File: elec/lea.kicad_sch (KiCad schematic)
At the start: 9 parts, among them J1 Servomoteur, J2 Screw_Terminal_01x02, J3 Jack, SW1 SW_SPDT

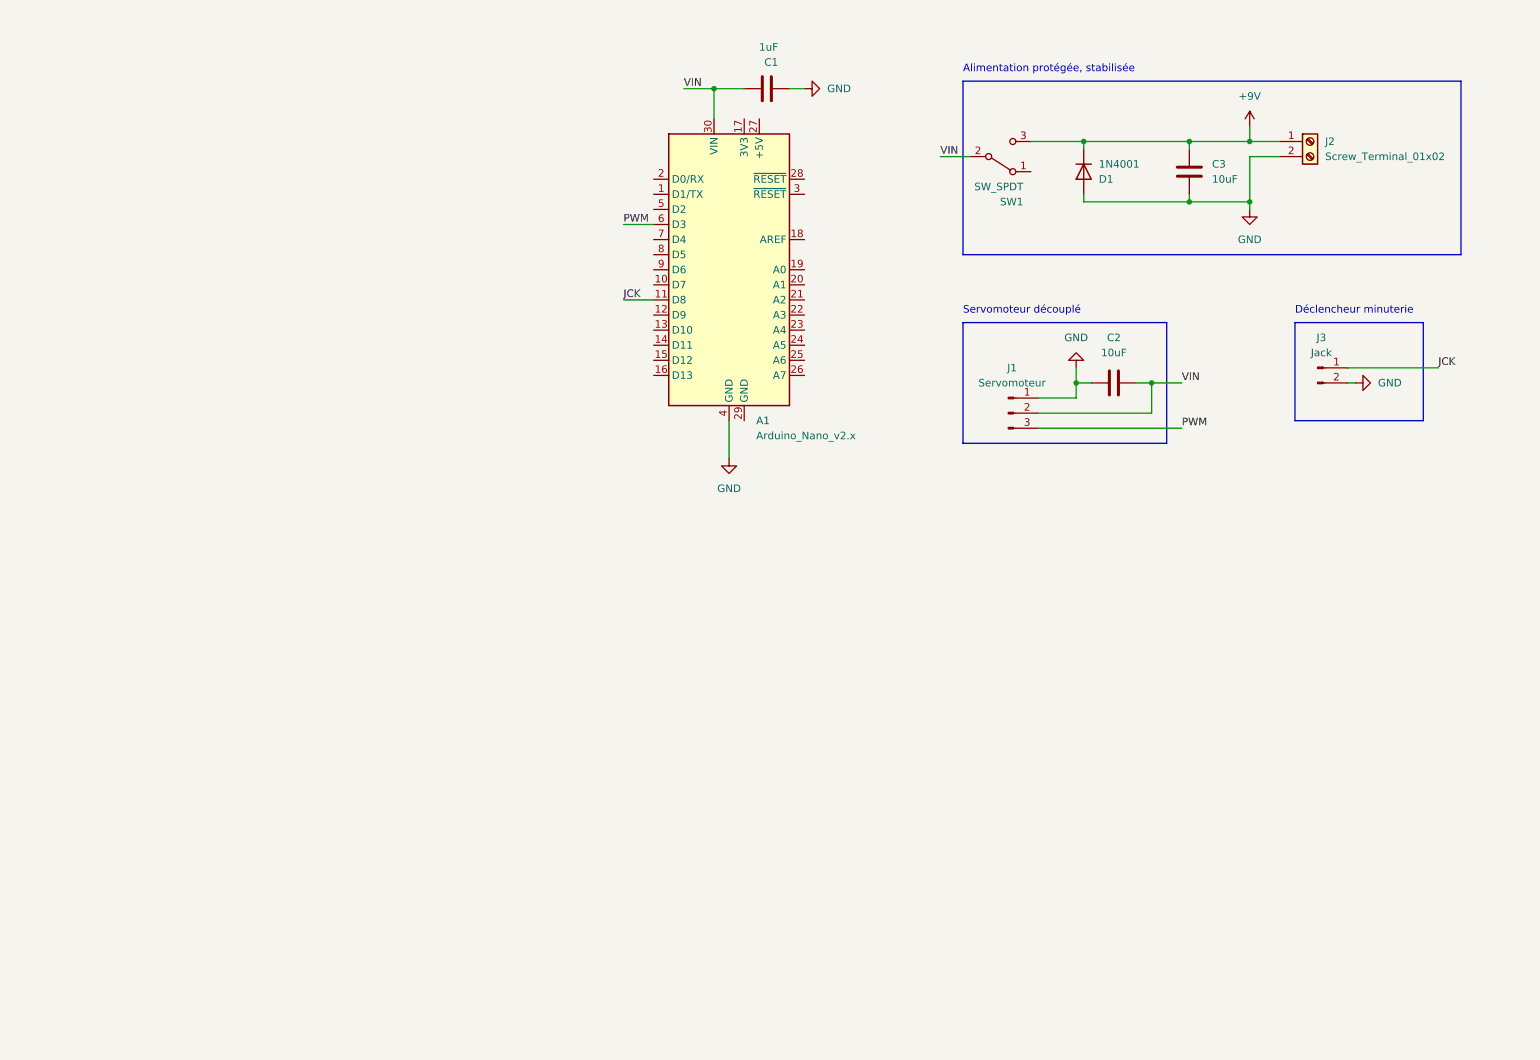
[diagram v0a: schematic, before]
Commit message: Refonte complète du circuit
- réagencement des composants sur le schéma
- pcb désormais rectangulaire
- ajout du régulateur de tension et de son empreinte
- masses séparées avec possibilité de pont
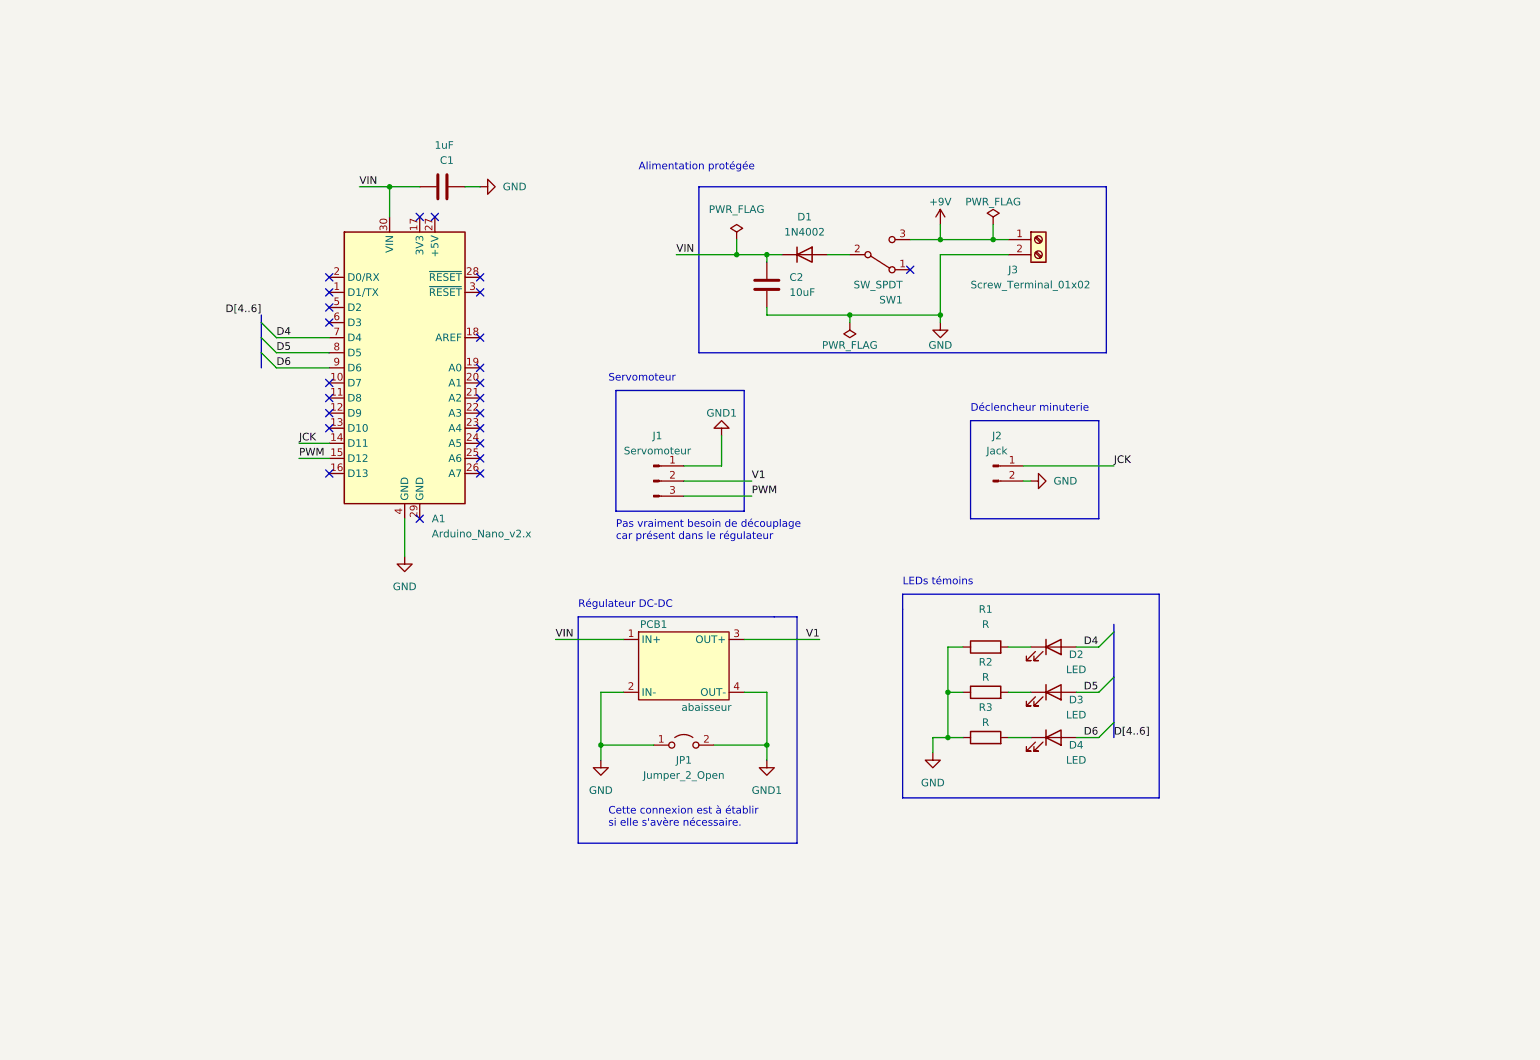
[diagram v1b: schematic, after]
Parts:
- removed C2: 10uF, Capacitor_THT:C_Radial_D6.3mm_H5.0mm_P2.50mm, symbol Device:C
- removed D1: 1N4001, Diode_THT:D_DO-41_SOD81_P10.16mm_Horizontal, symbol Diode:1N4001
- added D1: 1N4002, Diode_THT:D_DO-41_SOD81_P10.16mm_Horizontal, symbol Diode:1N4002
- added D2, D3, D4: LED, LED_THT:LED_D5.0mm, symbol Device:LED
- added JP1: Jumper_2_Open, Connector_PinSocket_2.54mm:PinSocket_1x02_P2.54mm_Vertical, symbol Jumper:Jumper_2_Open
- added PCB1: abaisseur, meiVestigii:abaisseur_TOP-AERO, symbol meus_signi:abaisseur
- added R1, R2, R3: R, Resistor_THT:R_Axial_DIN0309_L9.0mm_D3.2mm_P12.70mm_Horizontal, symbol Device:R
- SW1: footprint Button_Switch_THT:SW_E-Switch_EG1224_SPDT_Angled -> Button_Switch_THT:SW_Slide_1P2T_CK_OS102011MS2Q
- renumbered C3 to C2, J3 to J2, J2 to J3
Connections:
- net +9V: no longer C2.2
- net GND: now also JP1.1 (A), PCB1.2 (IN-), R1.1, R2.1, R3.1; no longer J1.1 (Pin_1)
- net JCK: now also A1.14 (D11); no longer A1.11 (D8)
- net PWM: now also A1.15 (D12); no longer A1.6 (D3)
- net VIN: now also C2.2, D1.1 (K), PCB1.1 (IN+); no longer J1.2 (Pin_2), SW1.2 (B)
- net D4: now reaches A1.7 (D4)
- net D4: now also D2.2 (A)
- net D5: now reaches A1.8 (D5)
- net D5: now also D3.2 (A)
- net D6: now reaches A1.9 (D6)
- net D6: now also D4.2 (A)
- new net: D1.2 (A), SW1.2 (B)
- new net: D4.1 (K), R3.2
- new net: D2.1 (K), R1.2
- new net: D3.1 (K), R2.2
- new net GND1: J1.1 (Pin_1), JP1.2 (B), PCB1.4 (OUT-)
- new net V1: J1.2 (Pin_2), PCB1.3 (OUT+)
- no-connect marks 0 -> 24
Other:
- note added: "Alimentation protégée"
- note added: "Cette connexion est à établir si elle s'avère nécessaire."
- note added: "LEDs témoins"
- note added: "Pas vraiment besoin de découplage car présent dans le régulateur"
- note added: "Régulateur DC-DC"
- note added: "Servomoteur"
- note removed: "Alimentation protégée, stabilisée"
- note removed: "Servomoteur découplé"
- moved on the sheet: A1, C1, C2, J1, J2, J3, SW1

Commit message: version du pcb usinable au fablab
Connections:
- net GND: now also J2.1 (Pin_1); no longer J2.2 (Pin_2)
- net JCK: now also A1.5 (D2), J2.2 (Pin_2); no longer A1.14 (D11), J2.1 (Pin_1)
- net PWM: now also A1.6 (D3); no longer A1.15 (D12)
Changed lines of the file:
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@@
   (no_connect (at 173.99 59.69))
   (no_connect (at 76.2 63.5))
-  (no_connect (at 76.2 66.04))
+  (no_connect (at 76.2 88.9))
   (no_connect (at 76.2 60.96))
-  (no_connect (at 76.2 68.58))
+  (no_connect (at 76.2 91.44))
   (no_connect (at 91.44 50.8))
   (no_connect (at 101.6 76.2))
@@
     (stroke (width 0) (type default) (color 0 0 0 0))
   )
-  (wire (pts (xy 71.12 88.9) (xy 76.2 88.9))
+  (wire (pts (xy 71.12 66.04) (xy 76.2 66.04))
     (stroke (width 0) (type default) (color 0 0 0 0))
   )
@@
     (stroke (width 0) (type default) (color 0 0 0 0))
   )
-  (wire (pts (xy 71.12 91.44) (xy 76.2 91.44))
+  (wire (pts (xy 71.12 68.58) (xy 76.2 68.58))
     (stroke (width 0) (type default) (color 0 0 0 0))
   )
@@
     (effects (font (size 1.27 1.27)) (justify left bottom))
   )
-  (label "JCK" (at 71.12 88.9 0)
+  (label "JCK" (at 71.12 66.04 0)
     (effects (font (size 1.27 1.27)) (justify left bottom))
   )
@@
     (effects (font (size 1.27 1.27)) (justify right bottom))
   )
-  (label "PWM" (at 71.12 91.44 0)
+  (label "PWM" (at 71.12 68.58 0)
     (effects (font (size 1.27 1.27)) (justify left bottom))
   )
@@
     (pin "2")
   )
-  (symbol (lib_id "Connector:Conn_01x02_Male") (at 187.96 92.71 0) (unit 1)
-    (in_bom yes) (on_board yes)
-    (property "Reference" "J2" (id 0) (at 188.595 87.63 0))
-    (property "Value" "Jack" (id 1) (at 188.595 90.17 0))
-    (property "Footprint" "Connector_JST:JST_XH_B2B-XH-A_1x02_P2.50mm_Vertical" (id 2) (at 187.96 92.71 0)
-      (effects (font (size 1.27 1.27)) hide)
-    )
-    (property "Datasheet" "~" (id 3) (at 187.96 92.71 0)
-      (effects (font (size 1.27 1.27)) hide)
-    )
+  (symbol (lib_id "Connector:Conn_01x02_Male") (at 187.96 95.25 0) (mirror x) (unit 1)
+    (in_bom yes) (on_board yes)
+    (property "Reference" "J2" (id 0) (at 188.595 100.33 0))
+    (property "Value" "Jack" (id 1) (at 188.595 97.79 0))
+    (property "Footprint" "Connector_JST:JST_XH_B2B-XH-A_1x02_P2.50mm_Vertical" (id 2) (at 187.96 95.25 0)
+      (effects (font (size 1.27 1.27)) hide)
+    )
+    (property "Datasheet" "~" (id 3) (at 187.96 95.25 0)
+      (effects (font (size 1.27 1.27)) hide)
+    )

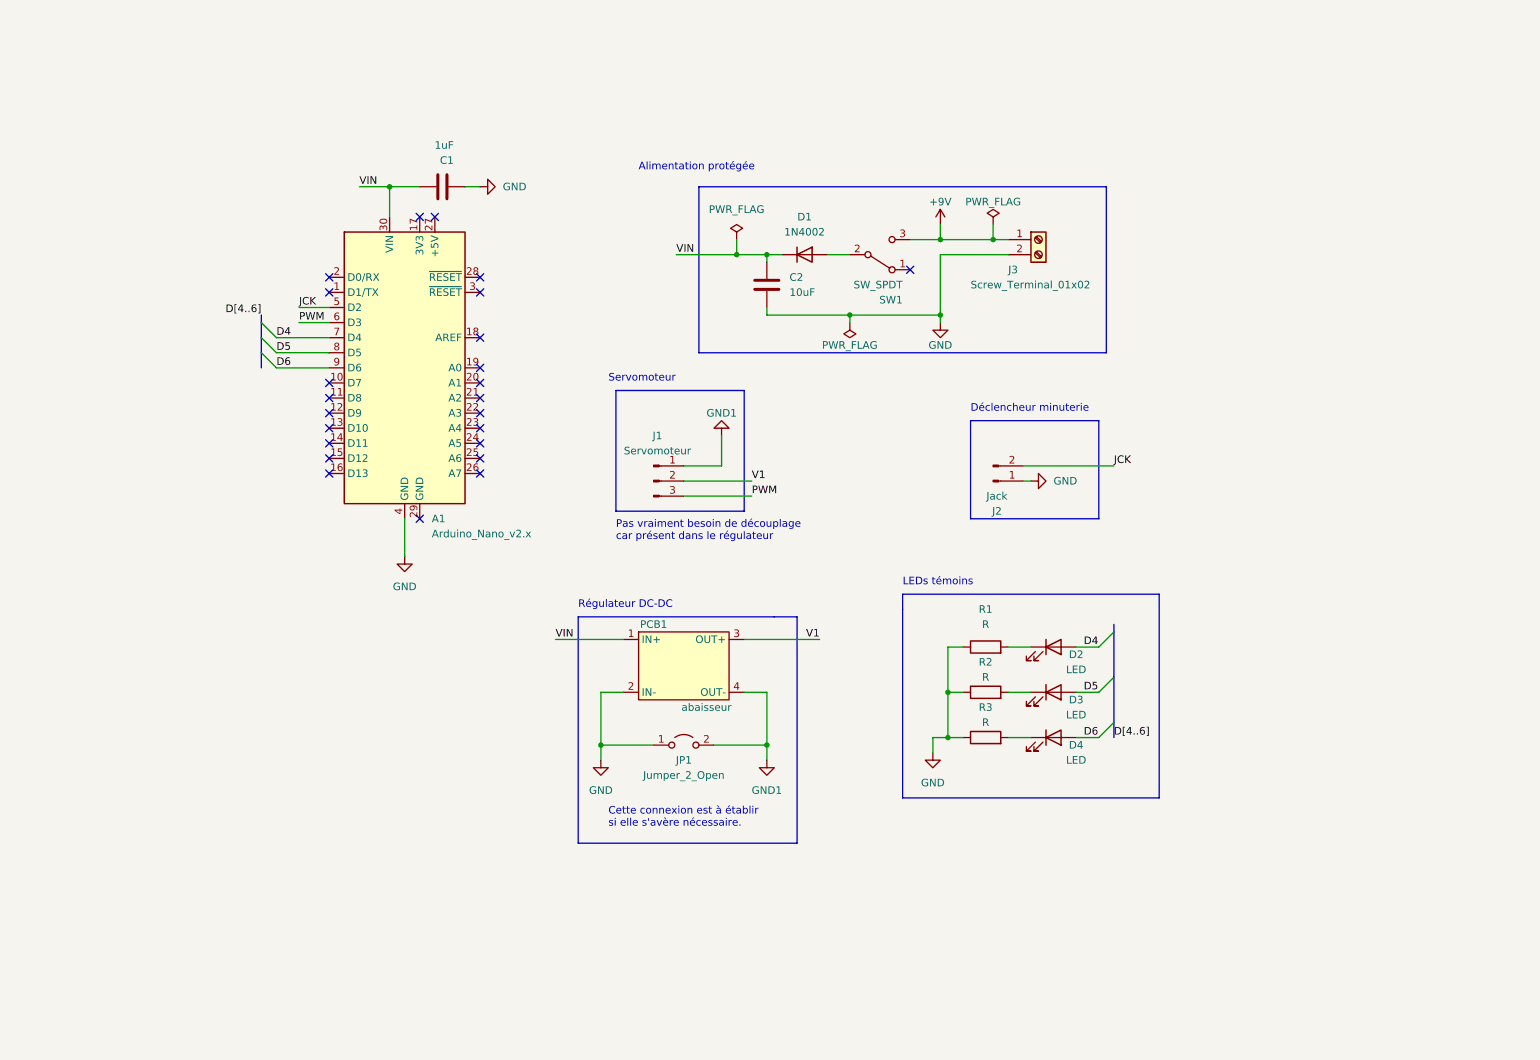
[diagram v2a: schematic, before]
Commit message: switch dorénavant au format dip et nouveeau schéma pour circuit bonus
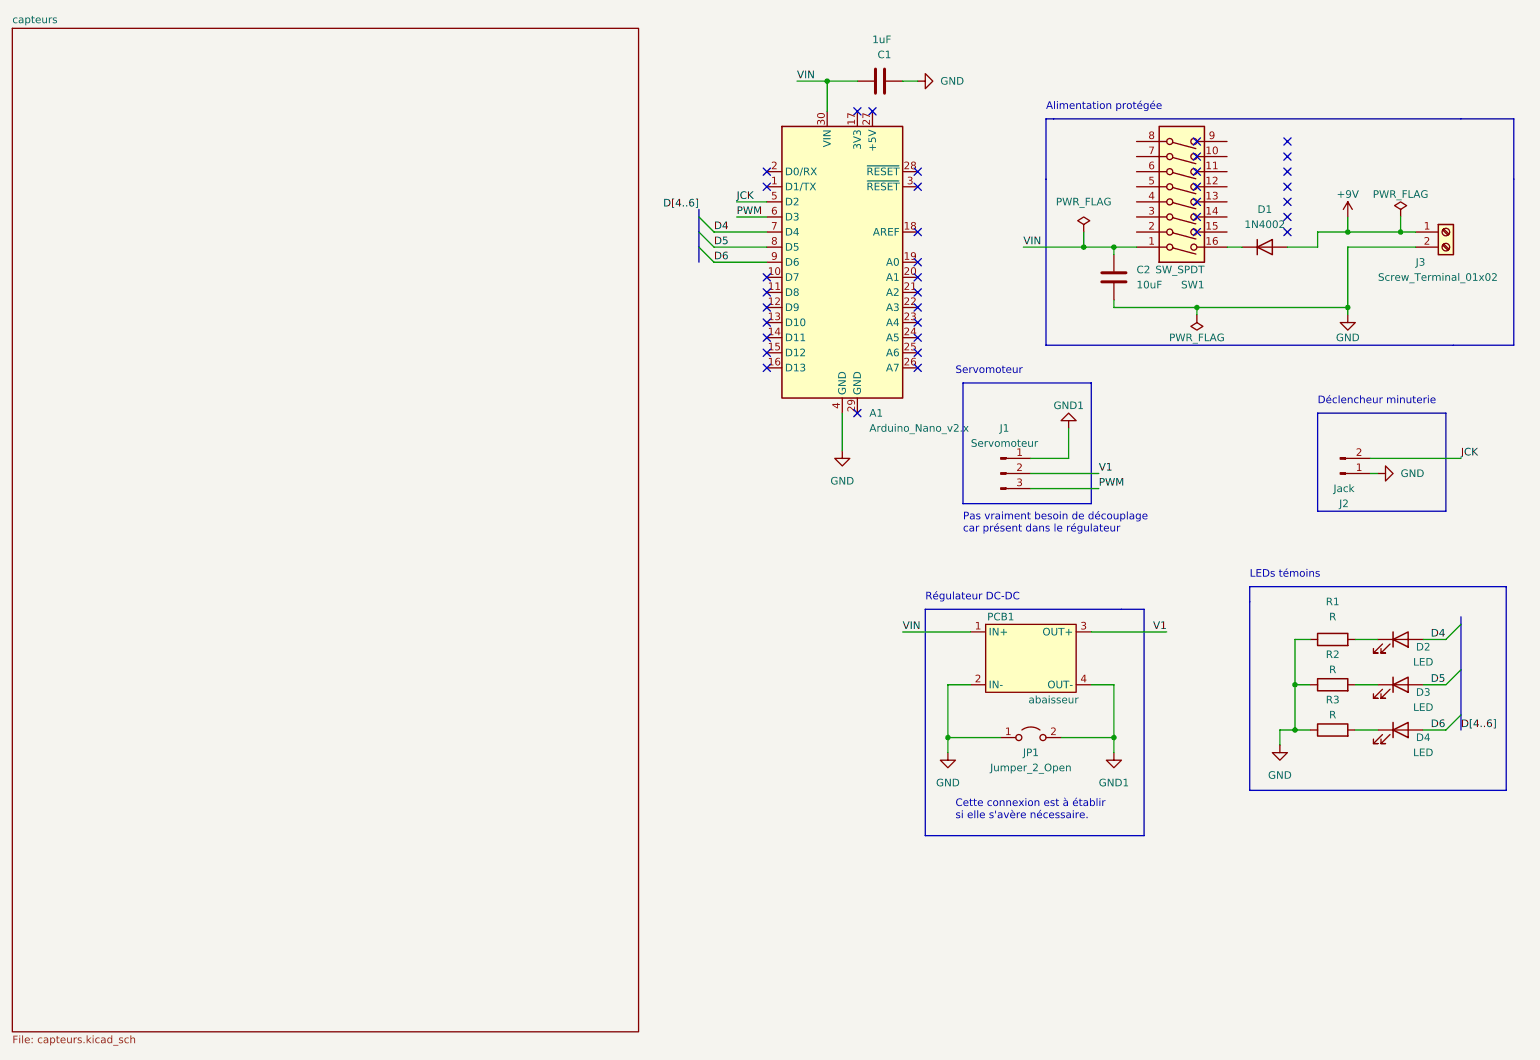
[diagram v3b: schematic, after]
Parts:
- SW1: footprint Button_Switch_THT:SW_Slide_1P2T_CK_OS102011MS2Q -> Button_Switch_THT:SW_DIP_SPSTx08_Slide_9.78x22.5mm_W7.62mm_P2.54mm; symbol Switch:SW_SPDT -> Switch:SW_DIP_x08
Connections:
- net +9V: now also D1.2 (A); no longer SW1.3 (C)
- net VIN: now also SW1.1; no longer D1.1 (K)
- net at SW1.2: no longer D1.2 (A)
- new net: D1.1 (K), SW1.16
- no-connect marks 24 -> 37
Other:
- added sheet capteurs (capteurs.kicad_sch)
- moved on the sheet: A1, C1, C2, D1, D2, D3, D4, J1, J2, J3, JP1, PCB1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
